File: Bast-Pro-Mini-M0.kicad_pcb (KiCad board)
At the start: 2 copper layers, 17.8 x 33 mm, 23 parts, among them J1 USB_B_Micro, J2 Conn_02x02_Odd_Even, P1 Digital, P2 ADC, P4 Analog, SW1 SW_DPST_x2, U1 AP2112K-3.3TRG1, U2 ATSAMD21E18A-AF

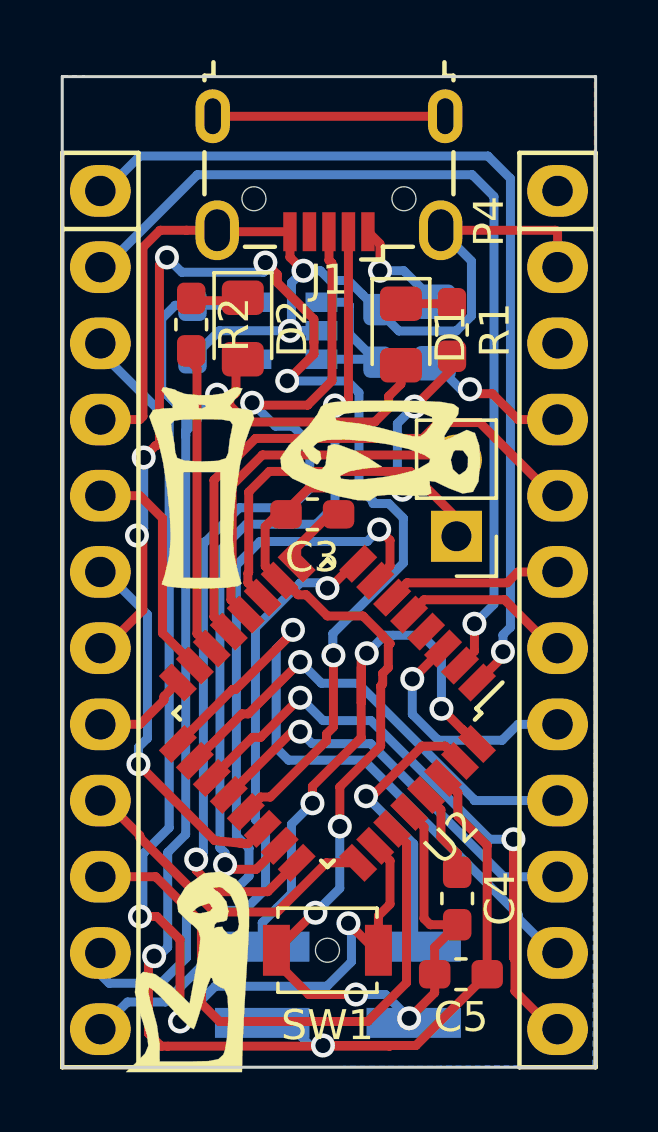
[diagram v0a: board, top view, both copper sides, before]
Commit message: silkscreen number pins
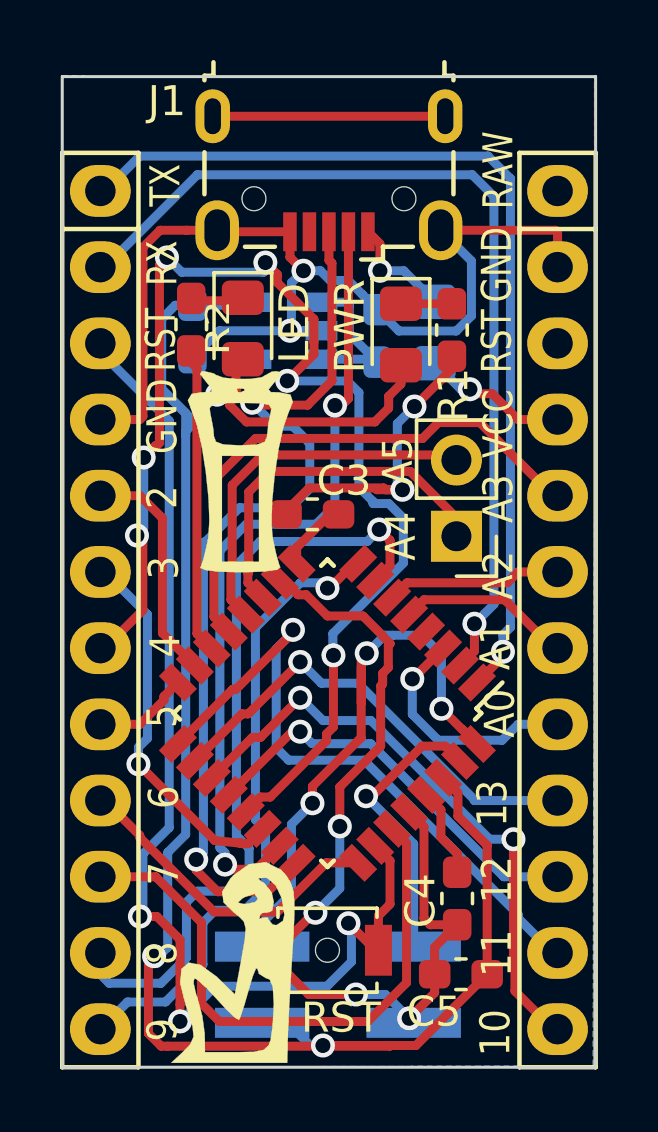
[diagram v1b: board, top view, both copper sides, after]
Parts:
- added G***: LOGO, LOGO, B.Cu at (142.4, 96.7)
- G***: moved to B.Cu
- moved G*** 9.66 mm to (146.4, 84.1), turned to 180 degrees
- moved G*** 1.54 mm to (142.8, 110.8)
- moved G*** 1.40 mm to (143.1, 94.5)
- moved G*** 0.60 mm to (143.2, 105.2)
- renumbered D2 to LED, D1 to PWR, SW1 to RST
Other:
- board text added: "10"
- board text added: "11"
- board text added: "12"
- board text added: "13"
- board text added: "2"
- board text added: "3"
- board text added: "3V3"
- board text added: "4"
- board text added: "5"
- board text added: "6"
- board text added: "7"
- board text added: "8"
- board text added: "9"
- board text added: "A0"
- board text added: "A1"
- board text added: "A2"
- board text added: "A3"
- board text added: "A4"
- board text added: "A5"
- board text added: "CLK"
- board text added: "DIO"
- board text added: "GND"
- board text added: "RAW"
- board text added: "RST"
- board text added: "RX"
- board text added: "TX"
- board text added: "VCC"

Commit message: Fix details
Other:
- board text added: "."
